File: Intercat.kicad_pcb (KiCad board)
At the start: 2 copper layers, 96 parts, among them J1 Conn_01x03, J2 Conn_01x03, J3 DE9_Receptacle, J4 USB_C_Receptacle_USB2.0, SW1 SW_Push, T1 LM-NP-1001-B1L, T2 LM-NP-1001-B1L, T3 LM-NP-1001-B1L, T4 LM-NP-1001-B1L, U1 CP2615-xx-xM, U10 MAX3250, U11 TLP185, U12 TLP185, U2 USBLC6-2SC6, U3 PCM3060, U4 MCP6002, U5 MCP6002, U6 MCP6002, U8 TLP185, U9 TLP185

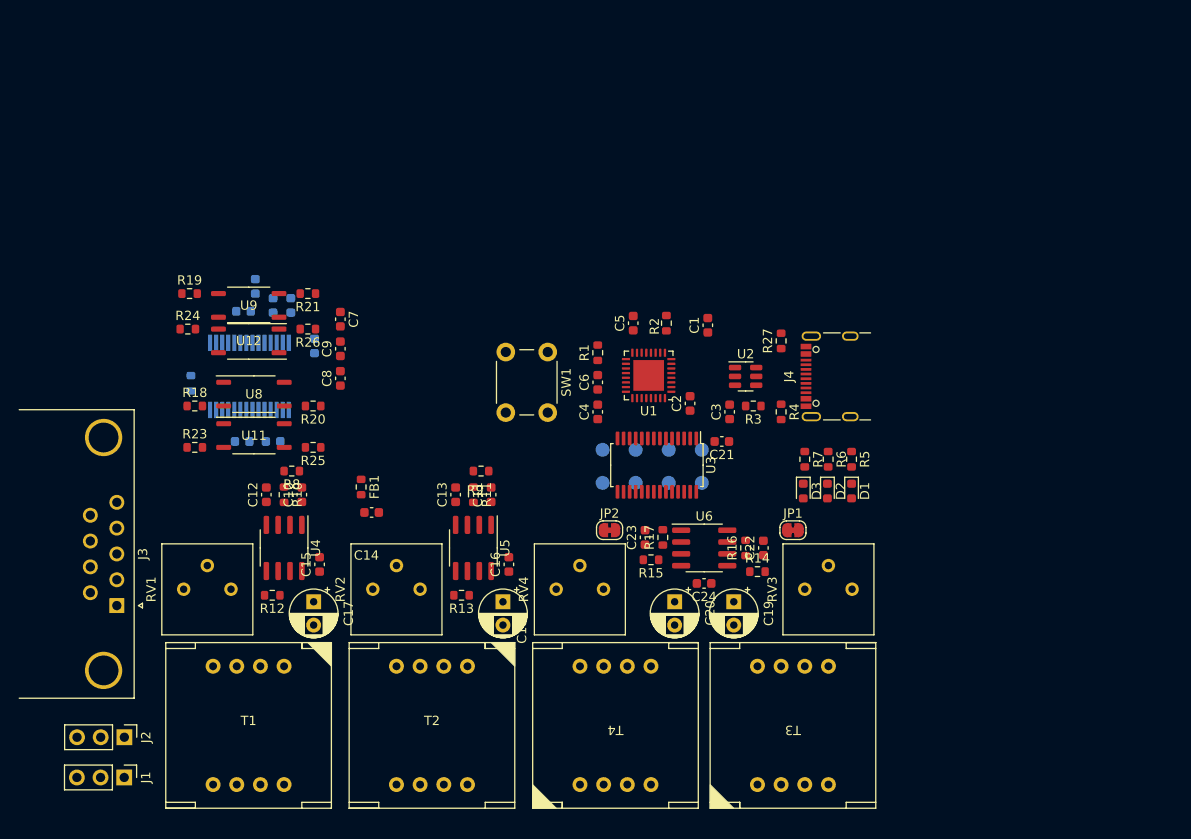
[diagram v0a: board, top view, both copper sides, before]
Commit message: added edge cuts, smaller PCB, bugfix
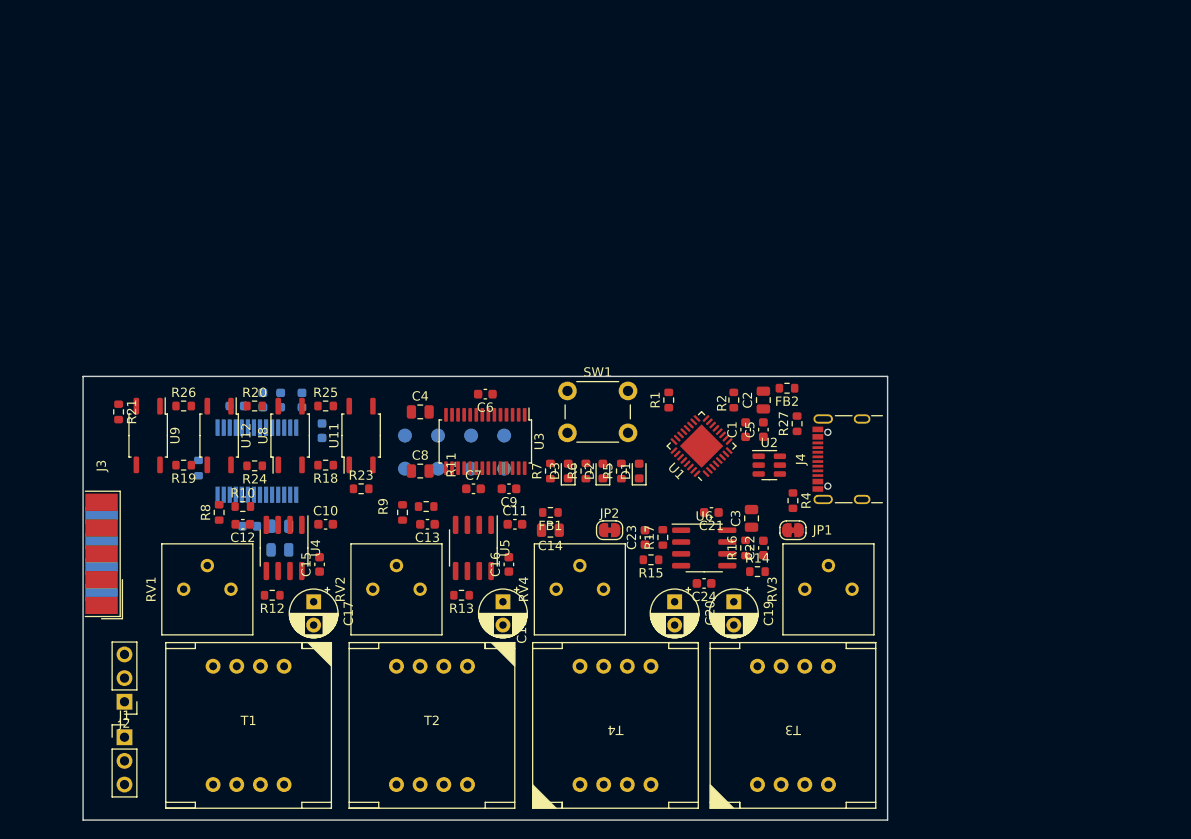
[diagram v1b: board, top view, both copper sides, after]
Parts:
- removed R3: R, Resistor_SMD:R_0603_1608Metric
- added C32: 1u, Capacitor_SMD:C_0805_2012Metric, B.Cu at (84.6, 119.0)
- added FB2: FerriteBead, Resistor_SMD:R_0603_1608Metric, F.Cu at (139.1, 101.6)
- C14, C2, C3, C4, C8: value 1uF -> 1u; footprint Capacitor_SMD:C_0603_1608Metric -> Capacitor_SMD:C_0805_2012Metric
- C27: value C -> 1u; footprint Capacitor_SMD:C_0603_1608Metric -> Capacitor_SMD:C_0805_2012Metric
- J3: footprint Connector_Dsub:DSUB-9_Female_Horizontal_P2.77x2.84mm_EdgePinOffset7.70mm_Housed_MountingHolesOffset9.12mm -> Connector_Dsub:DSUB-9_Female_EdgeMount_P2.77mm
- R18, R19, R20, R21, R22, R23, R24, R25, R26, R5, R6, R7: value R -> 1k
- U11, U12, U8, U9: value TLP185 -> EL357N(C)(TA)-G; footprint Package_SO:SOIC-4_4.55x3.7mm_P2.54mm -> Package_SO:SO-4_4.4x3.9mm_P2.54mm
- moved R7 27.3 mm to (113.7, 110.5), turned to 90 degrees
- moved R6 26.0 mm to (117.5, 110.5), turned to 90 degrees
- moved D3 25.3 mm to (115.6, 110.5), turned to 90 degrees
- moved R5 24.7 mm to (121.3, 110.5), turned to 90 degrees
- moved D2 24.2 mm to (119.3, 110.5), turned to 90 degrees
- moved R21 24.0 mm to (67.3, 104.1), turned to -90 degrees
- moved C9 23.5 mm to (109.2, 112.4), turned to 180 degrees
- moved C7 23.1 mm to (105.4, 112.4), turned to 0 degrees
- moved D1 22.9 mm to (123.2, 110.5), turned to 90 degrees
- moved TP5 21.3 mm to (101.6, 106.7)
- moved TP6 21.3 mm to (101.6, 110.2)
- moved TP7 21.3 mm to (98.0, 106.7)
- moved TP8 21.3 mm to (98.0, 110.2)
- moved TP2 21.3 mm to (108.7, 110.2)
- moved TP4 21.3 mm to (105.2, 110.2)
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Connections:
- R5 pad 1: /LED3 -> /CTS
- R6 pad 1: /LED2 -> /RTS
- R7 pad 1: /LED1 -> VBUS
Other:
- board outline added: 86.4 x 47.6 mm

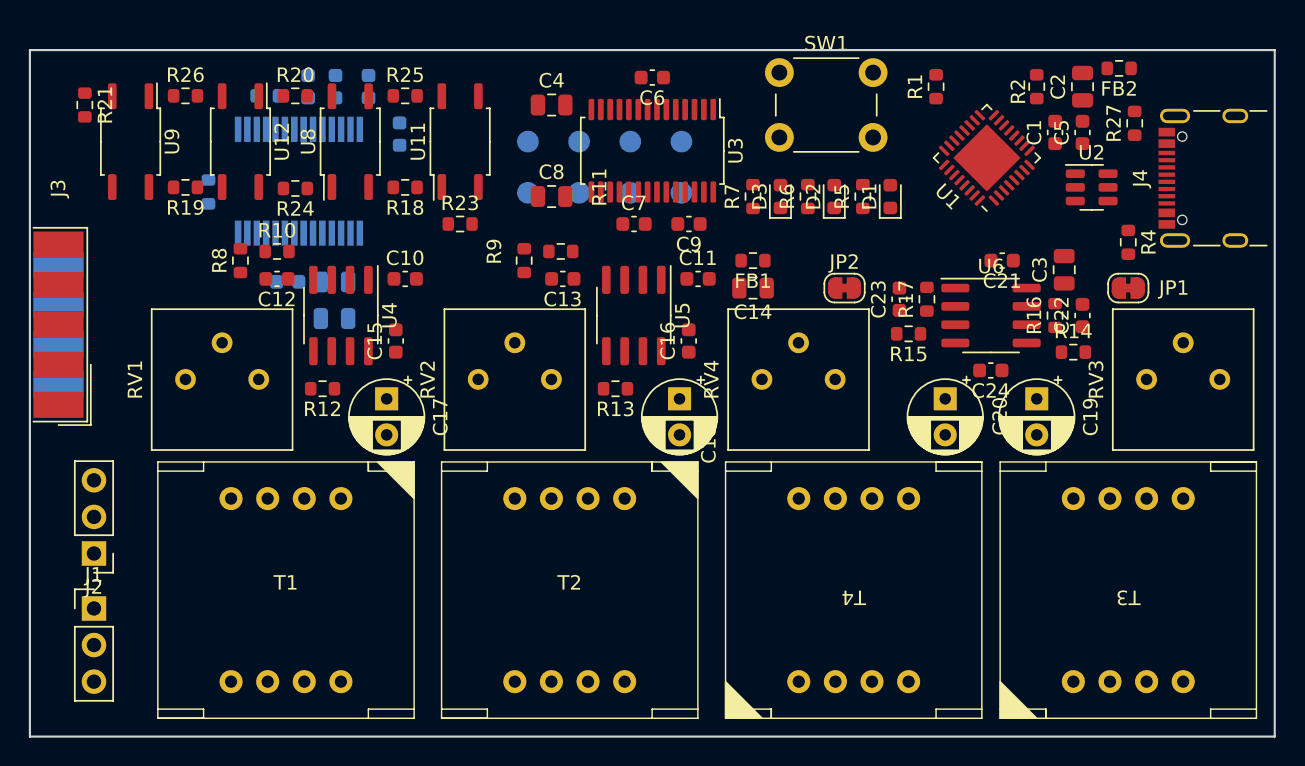
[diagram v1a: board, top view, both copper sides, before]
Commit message: changed 3d model of the transformer
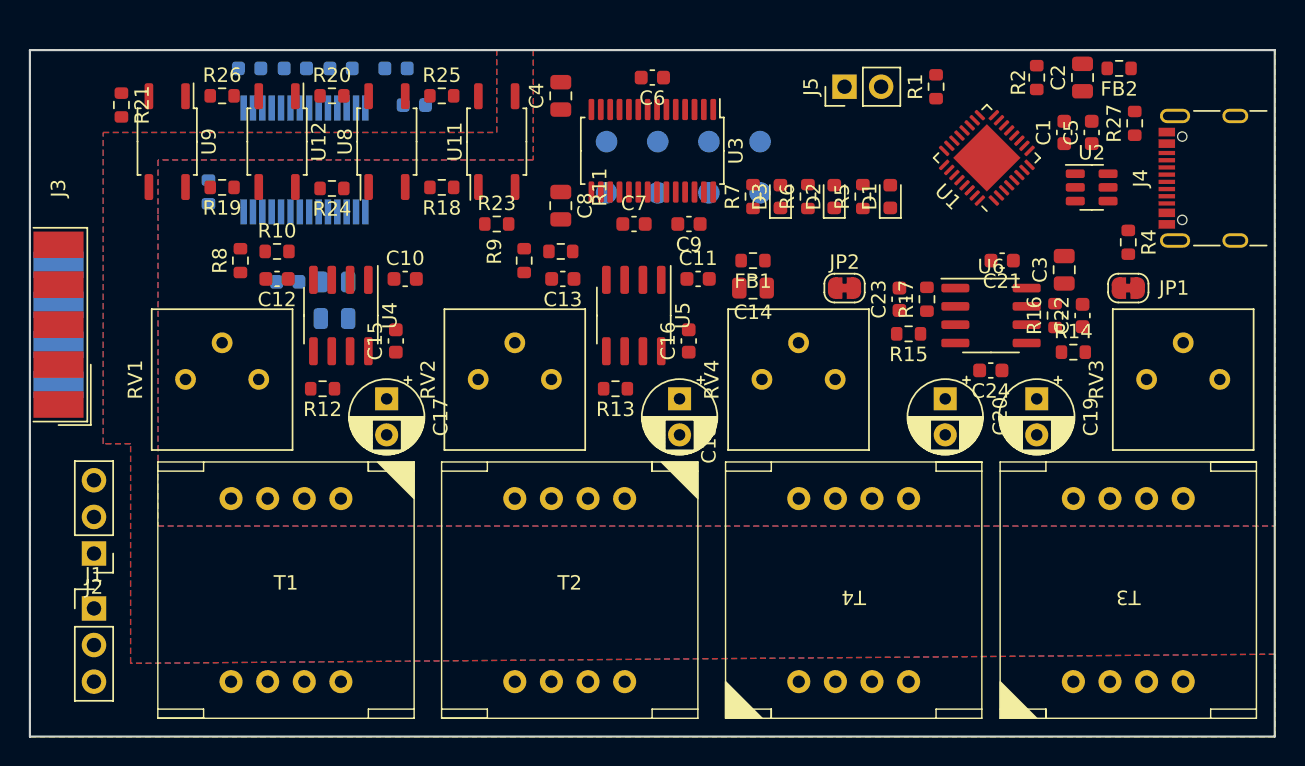
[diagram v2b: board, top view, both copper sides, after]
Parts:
- removed SW1: SW_Push, Button_Switch_THT:SW_PUSH_6mm
- added J5: Conn_01x02, Connector_PinHeader_2.54mm:PinHeader_1x02_P2.54mm_Vertical, F.Cu at (120.0, 102.9)
- moved TP5 5.46 mm to (107.1, 106.7)
- moved TP6 5.46 mm to (107.1, 110.2)
- moved TP1 5.45 mm to (114.2, 106.7)
- moved TP2 5.45 mm to (114.2, 110.2)
- moved TP3 5.45 mm to (110.6, 106.7)
- moved TP4 5.45 mm to (110.6, 110.2)
- moved TP7 5.45 mm to (103.5, 106.7)
- moved TP8 5.45 mm to (103.5, 110.2)
- moved R18 2.54 mm to (92.1, 109.9)
- moved R23 2.54 mm to (95.9, 112.4)
- moved R25 2.54 mm to (92.1, 103.5)
- moved U11 2.54 mm to (95.9, 106.7)
- moved U8 2.54 mm to (88.3, 106.7)
- moved U9 2.54 mm to (73.0, 106.7)
- moved R19 2.54 mm to (76.8, 109.9)
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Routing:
- added copper zone on B.Cu, net GND
- added copper zone on F.Cu, net GND
- added copper zone on B.Cu, net GNDA
- added copper zone on F.Cu, net GNDA

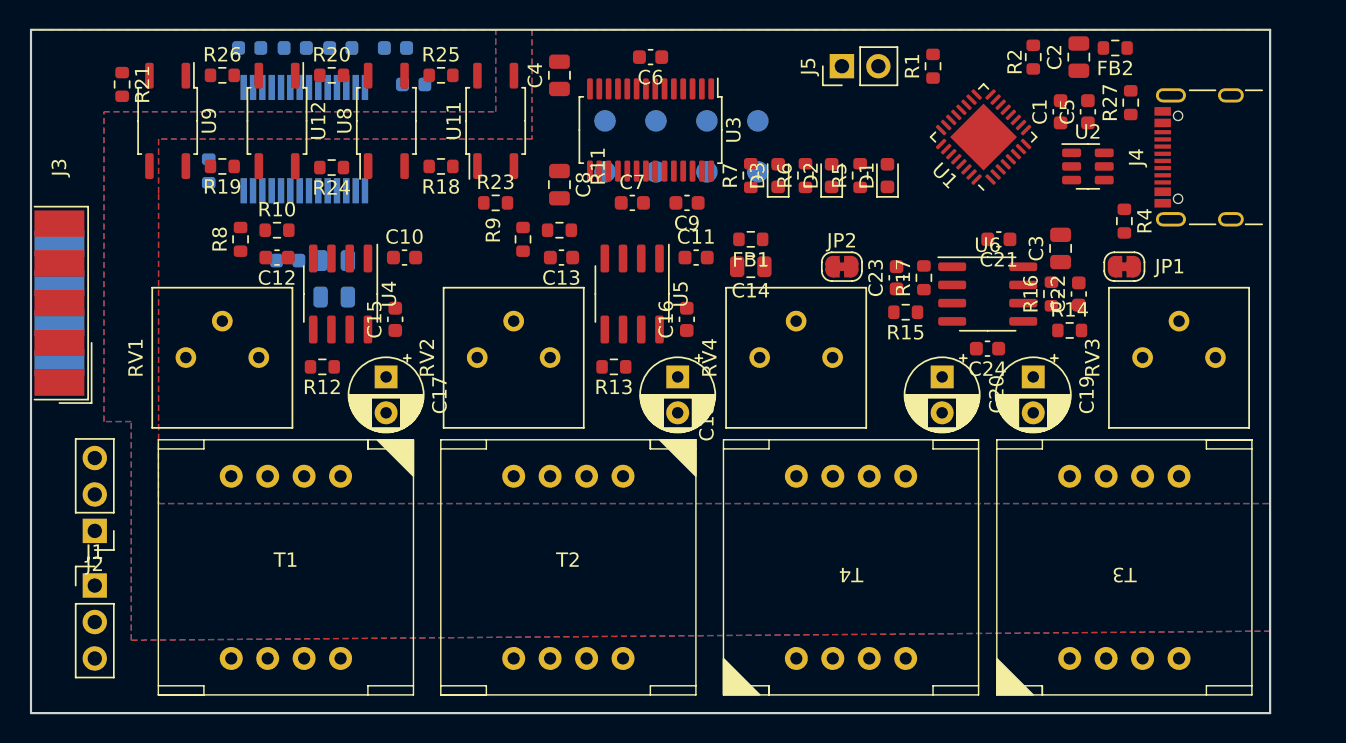
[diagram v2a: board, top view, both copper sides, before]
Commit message: reduced PCB size, started routing
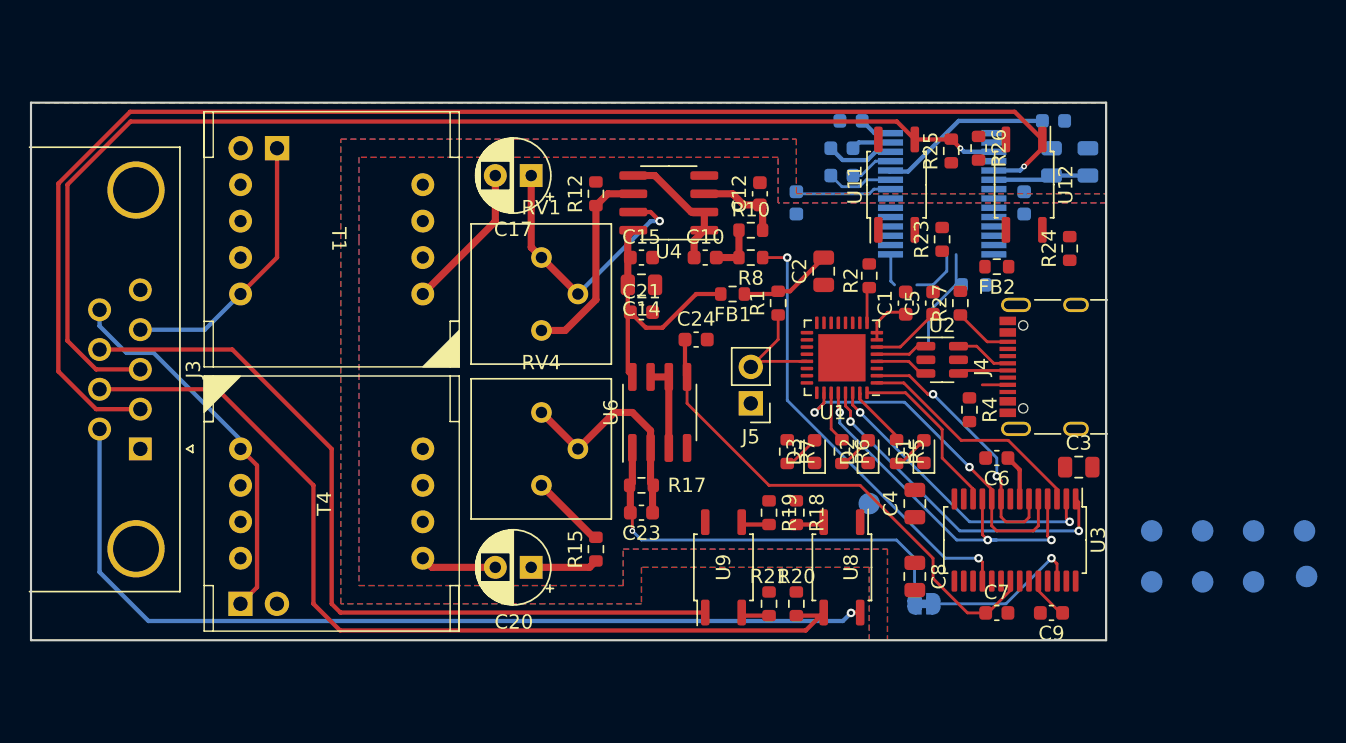
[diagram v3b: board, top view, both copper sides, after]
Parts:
- removed C11: 1n, Capacitor_SMD:C_0603_1608Metric
- removed C13, C22: 470p, Capacitor_SMD:C_0603_1608Metric
- removed C16: 100n, Capacitor_SMD:C_0603_1608Metric
- removed C18, C19: C_Polarized, Capacitor_THT:CP_Radial_D5.0mm_P2.50mm
- removed JP1: Jumper_2_Bridged, Jumper:SolderJumper-2_P1.3mm_Bridged_RoundedPad1.0x1.5mm
- removed R11, R14: 3k9, Resistor_SMD:R_0603_1608Metric
- removed R13, R16, R9: 9k1, Resistor_SMD:R_0603_1608Metric
- removed RV2, RV3: 10k, Potentiometer_THT:Potentiometer_Bourns_3386P_Vertical
- removed T2, T3: LM-NP-1001-B1L, InterCat:LM-NP-1001-B1L
- removed U5: MCP6002, Package_SO:SOIC-8_3.9x4.9mm_P1.27mm
- added TP19: TestPoint, TestPoint:TestPoint_Pad_D1.5mm, B.Cu at (121.9, 133.3)
- J1, J2: value Conn_01x03 -> Conn_01x02; footprint Connector_PinHeader_2.54mm:PinHeader_1x03_P2.54mm_Vertical -> Connector_PinHeader_2.54mm:PinHeader_1x02_P2.54mm_Vertical; moved to B.Cu
- J3: footprint Connector_Dsub:DSUB-9_Female_EdgeMount_P2.77mm -> Connector_Dsub:DSUB-9_Female_Horizontal_P2.77x2.84mm_EdgePinOffset4.94mm_Housed_MountingHolesOffset7.48mm
- JP2: moved to B.Cu
- U11, U12, U8, U9: footprint Package_SO:SO-4_4.4x3.9mm_P2.54mm -> InterCat:SO-6-4_4.4x3.9mm_P2.54mm
- moved R21 57.8 mm to (114.9, 140.3)
- moved R22 53.9 mm to (129.2, 118.1), turned to 0 degrees
- moved C32 53.4 mm to (137.2, 109.5), turned to 90 degrees
- moved C28 53.1 mm to (134.8, 106.7), turned to 0 degrees
- moved R26 52.9 mm to (129.5, 108.6), turned to -90 degrees
- moved U12 52.3 mm to (132.7, 111.1)
- moved R24 51.7 mm to (135.9, 115.6), turned to 90 degrees
- moved C25 51.5 mm to (132.7, 112.4), turned to -90 degrees
- moved C27 50.5 mm to (134.6, 109.5), turned to 90 degrees
- moved U9 49.7 mm to (111.8, 137.8), turned to 90 degrees
- moved R20 49.0 mm to (116.8, 140.3), turned to -90 degrees
- moved TP4 47.6 mm to (148.7, 138.8)
- moved TP3 47.6 mm to (148.7, 135.3)
- moved TP6 47.6 mm to (145.2, 138.8)
- moved TP8 47.6 mm to (141.6, 138.8)
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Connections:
- J1 pad 1: GNDA -> /OUT_ISO
- J1 pad 2: /OUT_ISO -> GNDA
- J2 pad 1: GNDA -> /IN_ISO
- J2 pad 2: /IN_ISO -> GNDA
- U6 pad 3: /DAC_Vref -> /Analog Filter/Vref#
- U6 pad 6: Net-(U6B--) -> /Analog Filter/Vref#
- U6 pad 7: Net-(JP1-A) -> /Analog Filter/Vref#
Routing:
- net /RX_ISO: track 0.00 -> 96.0 mm, vias 0 -> 1
- net /TX_ISO: track 0.00 -> 84.1 mm, vias 0 -> 1
- net /RTS_ISO: track 0.00 -> 64.8 mm
- net VS: track 0.00 -> 64.6 mm, vias 0 -> 1
- net /CTS_ISO: track 0.00 -> 56.1 mm
- net /DAC_Vref: track 0.00 -> 35.2 mm
- net /DAC_Rout: track 0.00 -> 31.3 mm, vias 0 -> 2
- net Net-(JP2-A): track 0.00 -> 29.6 mm, vias 0 -> 1
- net /LRCLK: track 0.00 -> 26.9 mm, vias 0 -> 3
- net /IN_ISO: track 0.00 -> 26.6 mm
- net /MCLK: track 0.00 -> 24.8 mm, vias 0 -> 2
- net /SCL: track 0.00 -> 23.5 mm, vias 0 -> 2
- net /SDA: track 0.00 -> 21.0 mm, vias 0 -> 2
- net Net-(C17-Pad1): track 0.00 -> 19.5 mm, vias 0 -> 1
- net /OUT_ISO: track 0.00 -> 19.2 mm
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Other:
- board size 86.4 x 47.6 mm -> 74.9 x 37.5 mm
